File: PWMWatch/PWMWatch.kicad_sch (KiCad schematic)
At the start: 22 parts, among them J1 USB_C_Receptacle_USB2.0_14P, SW1 RST, SW2 BOOT, U1 STM32WB50CGUx, U2 NCP1117-3.3_SOT223, U3 TVS1400DRV

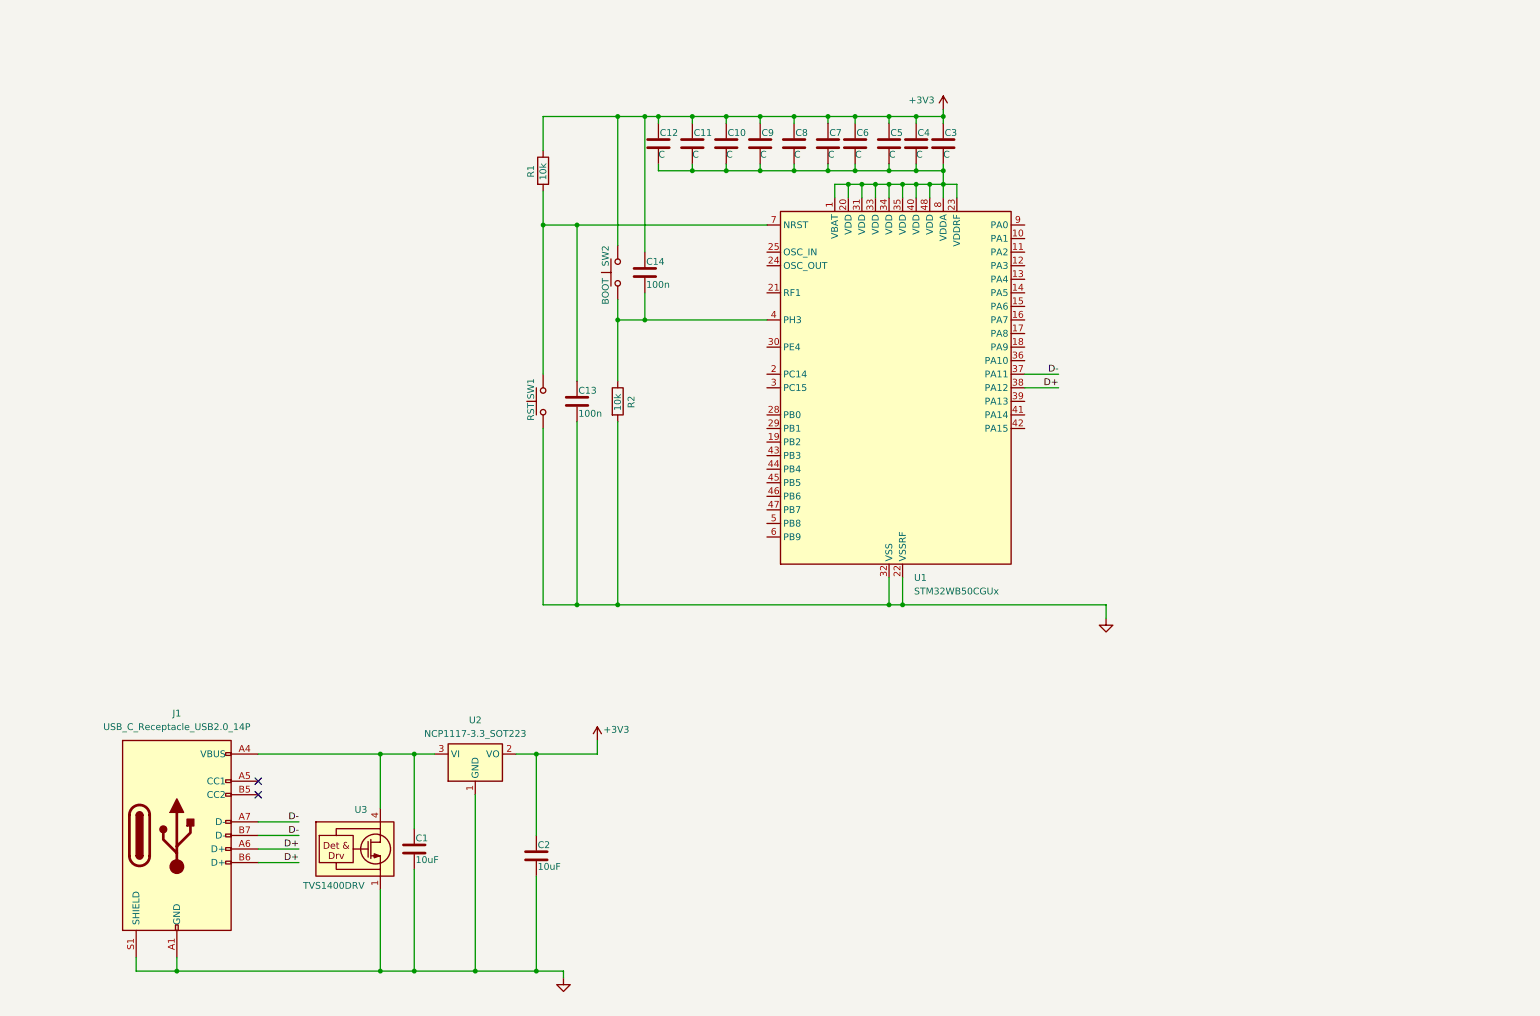
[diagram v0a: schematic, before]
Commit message: Added RTC
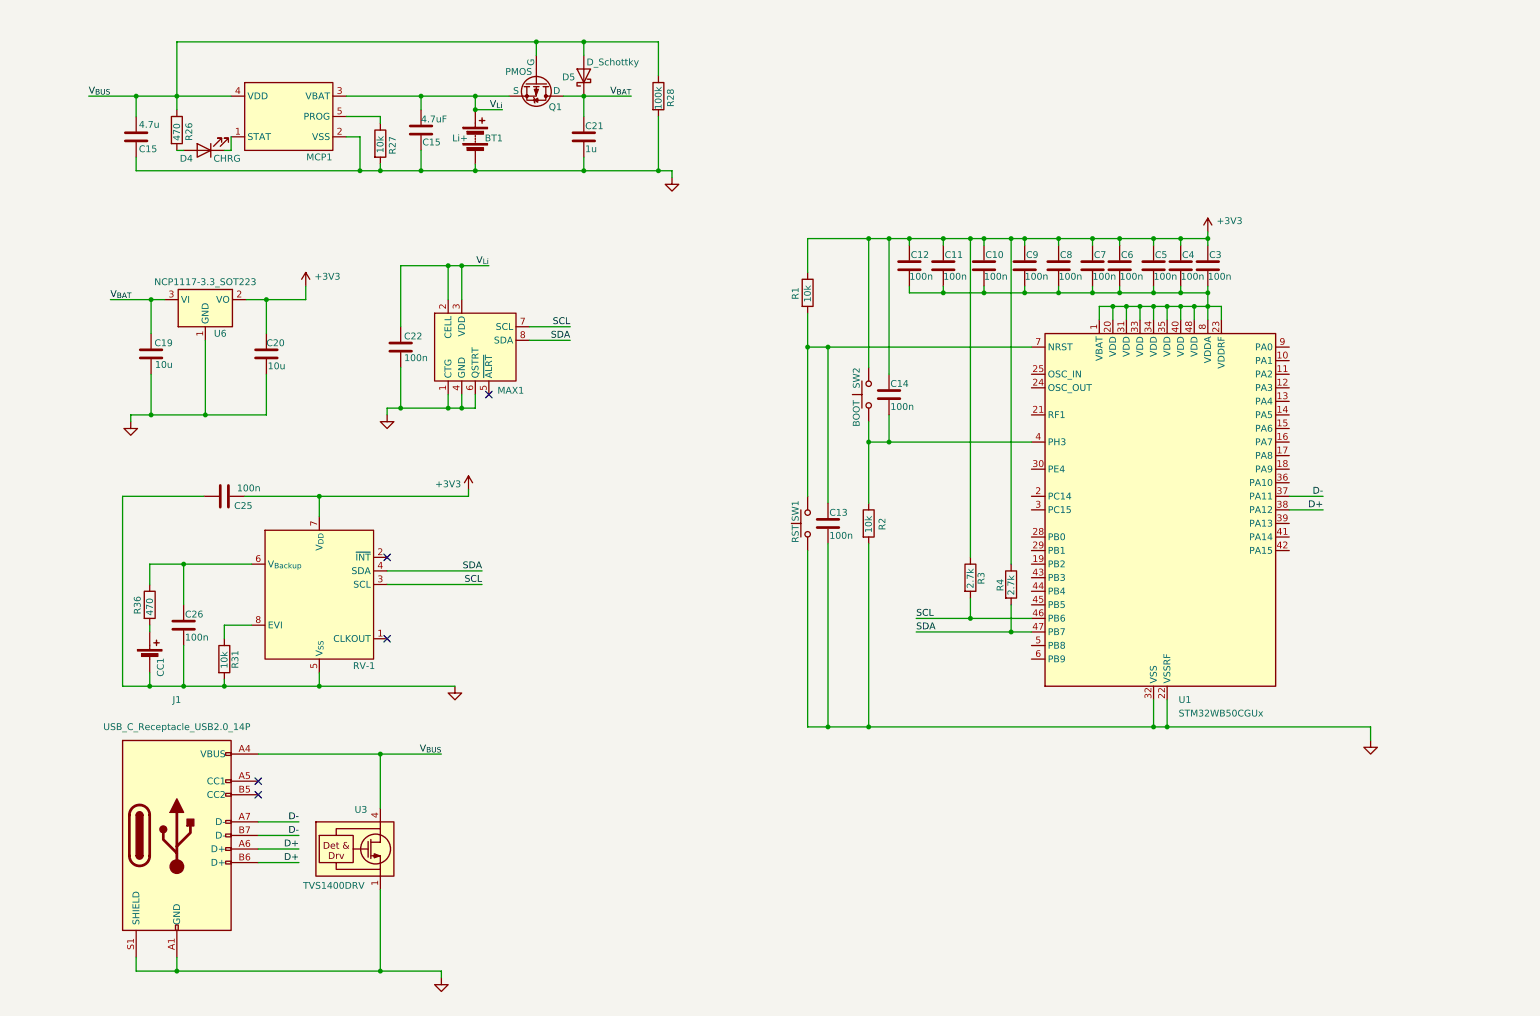
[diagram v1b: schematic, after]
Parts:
- removed C1, C2: 10uF, symbol Device:C
- removed U2: NCP1117-3.3_SOT223, Package_TO_SOT_SMD:SOT-223-3_TabPin2, symbol Regulator_Linear:NCP1117-3.3_SOT223
- added BT1: Li+, symbol Device:Battery
- added C15: 4.7u, Capacitor_SMD:C_0603_1608Metric, symbol Device:C
- added C15: 4.7uF, Capacitor_SMD:C_0603_1608Metric, symbol Device:C
- added C19, C20: 10u, Capacitor_SMD:C_0805_2012Metric, symbol Device:C
- added C21: 1u, Capacitor_SMD:C_0805_2012Metric, symbol Device:C
- added C22, C25, C26: 100n, Capacitor_SMD:C_0805_2012Metric, symbol Device:C
- added CC1: Battery_Cell, Uni:BAT_BK-414, symbol Device:Battery_Cell
- added D4: CHRG, LED_SMD:LED_0603_1608Metric, symbol Device:LED
- added D5: D_Schottky, Diode_SMD:D_SOD-123, symbol Device:D_Schottky
- added MAX1: ~, Package_DFN_QFN:TDFN-8-1EP_2x2mm_P0.5mm_EP0.8x1.2mm, symbol MAX17048:MAX17048
- added MCP1: ~, Package_TO_SOT_SMD:SOT-23-5, symbol MCP7383:MCP7383
- added Q1: PMOS, Package_TO_SOT_SMD:SOT-23-3, symbol Simulation_SPICE:PMOS
- added R26, R36: 470, Resistor_SMD:R_0603_1608Metric, symbol Device:R
- added R27, R31: 10k, Resistor_SMD:R_0603_1608Metric, symbol Device:R
- added R28: 100k, Resistor_SMD:R_0603_1608Metric, symbol Device:R
- added R3, R4: 2.7k, symbol Device:R
- added RV-1: ~, Uni:IC_RV-3028-C8-32.768KHZ-1PPM-TA-QC, symbol RV3028:RV-3028
- added U6: NCP1117-3.3_SOT223, Package_TO_SOT_SMD:SOT-223-3_TabPin2, symbol Regulator_Linear:NCP1117-3.3_SOT223
- C10, C11, C12, C3, C4, C5, C6, C7, C8, C9: value C -> 100n
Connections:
- net +3V3: now also C20.2, C25.2, R3.1, R4.1, RV-1.7 (V_{DD}), U6.2 (VO)
- net GND: now also BT1.2 (-), C15.2, C15.2, C19.1, C20.1, C21.2, C22.1, C25.1, C26.2, CC1.2 (-), MAX1.1 (CTG), MAX1.4 (GND), MAX1.6 (QSTRT), MCP1.2 (VSS), R27.2, R28.2, R31.2, RV-1.5 (V_{SS}), U6.1 (GND)
- net SCL: now reaches U1.46 (PB6)
- net SCL: now also MAX1.7 (SCL), R3.2, RV-1.3 (SCL)
- net SDA: now reaches U1.47 (PB7)
- net SDA: now also MAX1.8 (SDA), R4.2, RV-1.4 (SDA)
- net V_{BUS}: now reaches J1.A4 (VBUS), J1.A9 (VBUS), J1.B4 (VBUS), J1.B9 (VBUS), U3.4 (IN), U3.5 (IN), U3.6 (IN)
- net V_{BUS}: now also C15.1, D5.2 (A), MCP1.4 (VDD), Q1.2 (G), R26.1, R28.1
- new net: C26.1, R36.1, RV-1.6 (V_{Backup})
- new net: D4.1 (K), MCP1.1 (STAT)
- new net: D4.2 (A), R26.2
- new net: CC1.1 (+), R36.2
- new net: MCP1.5 (PROG), R27.1
- new net: R31.1, RV-1.8 (EVI)
- new net V_{BAT}: C19.2, C21.1, D5.1 (K), Q1.1 (D), U6.3 (VI)
- new net V_{Li}: BT1.1 (+), C15.1, C22.2, MAX1.2 (CELL), MAX1.3 (VDD), MCP1.3 (VBAT), Q1.3 (S)
- no-connect marks 2 -> 5
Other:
- moved on the sheet: C10, C11, C12, C13, C14, C3, C4, C5, C6, C7, C8, C9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

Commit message: magnetic encoder + buttons + organization of schematic
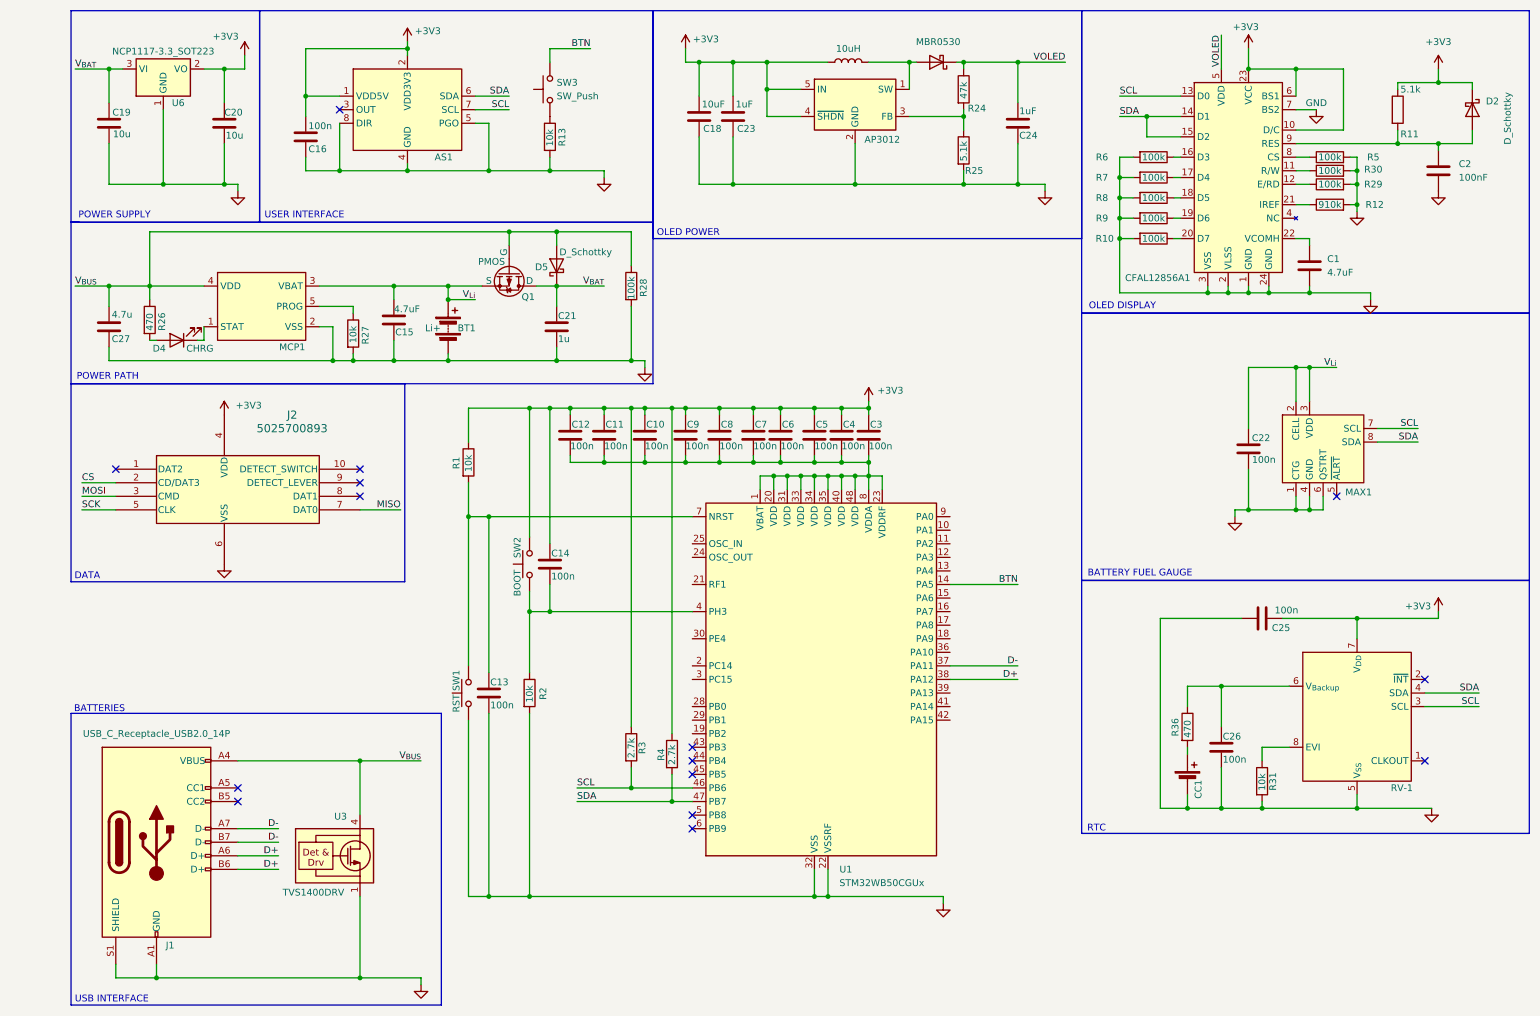
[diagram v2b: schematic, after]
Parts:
- added AS1: ~, Package_SO:SOIC-8_3.9x4.9mm_P1.27mm, symbol AS5600:AS5600
- added C1: 4.7uF, Capacitor_SMD:C_1206_3216Metric, symbol Device:C
- added C16: 100n, Capacitor_SMD:C_0805_2012Metric, symbol Device:C
- added C18: 10uF, Capacitor_SMD:C_0805_2012Metric, symbol Device:C
- added C2: 100nF, Capacitor_SMD:C_0805_2012Metric, symbol Device:C
- added C23, C24: 1uF, Capacitor_SMD:C_0805_2012Metric, symbol Device:C
- added CFAL12856A1: ~, Uni:GCT_FFC2A32-24-T, symbol CFAL128:CFAL128
- added D2: D_Schottky, Diode_SMD:D_SOD-523, symbol Device:D_Schottky
- added D6: MBR0530, Diode_SMD:D_SOD-123, symbol Diode:MBR0530
- added J2: 5025700893, Uni:GCT_MEM2061-01-188-00-A_REVA, symbol 2025-07-06_05-28-46:5025700893
- added L2: 10uH, Uni:IND_TAIYO_NRS4018_TAY, symbol Device:L
- added R10, R29, R30, R5, R6, R7, R8, R9: 100k, Resistor_SMD:R_0603_1608Metric, symbol Device:R
- added R11, R25: 5.1k, Resistor_SMD:R_0603_1608Metric, symbol Device:R
- added R12: 910k, Resistor_SMD:R_0603_1608Metric, symbol Device:R
- added R13: 10k, symbol Device:R
- added R24: 47k, Resistor_SMD:R_0603_1608Metric, symbol Device:R
- added SW3: SW_Push, symbol Switch:SW_Push
- added U2: AP3012, Package_TO_SOT_SMD:SC-74A-5_1.55x2.9mm_P0.95mm, symbol Regulator_Switching:AP3012
- C10, C11, C12, C13, C14, C3, C4, C5, C6, C7, C8, C9: footprint (none) -> Capacitor_SMD:C_0805_2012Metric
- R1, R2, R3, R4: footprint (none) -> Capacitor_SMD:C_0603_1608Metric
- renumbered C15 to C27
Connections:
- net +3V3: now also AS1.1 (VDD5V), AS1.2 (VDD3V3), C16.1, C18.1, C23.1, CFAL12856A1.10 (D/C), CFAL12856A1.23 (VCC), CFAL12856A1.6 (BS1), D2.1 (K), J2.4 (VDD), L2.1, R11.1, U2.4 (~{SHDN}), U2.5 (IN)
- net GND: now also AS1.4 (GND), AS1.5 (PGO), AS1.8 (DIR), C1.2, C16.2, C18.2, C2.2, C23.2, C24.2, CFAL12856A1.1 (GND), CFAL12856A1.2 (VLSS), CFAL12856A1.24 (GND), CFAL12856A1.3 (VSS), CFAL12856A1.7 (BS2), J2.6 (VSS), R10.2, R12.2, R13.2, R25.2, R29.2, R30.2, R5.2, R6.2, R7.2, R8.2, R9.2, U2.2 (GND)
- net SCL: now also AS1.7 (SCL), CFAL12856A1.13 (D0)
- net SDA: now also AS1.6 (SDA), CFAL12856A1.14 (D1), CFAL12856A1.15 (D2)
- net BTN: now reaches U1.14 (PA5)
- net BTN: now also SW3.2
- new net: C1.1, CFAL12856A1.22 (VCOMH)
- new net: D6.2 (A), L2.2, U2.1 (SW)
- new net: R24.2, R25.1, U2.3 (FB)
- new net: CFAL12856A1.17 (D4), R7.1
- new net: R13.1, SW3.1
- new net: CFAL12856A1.11 (R/W), R30.1
- new net: CFAL12856A1.12 (E/RD), R29.1
- new net: CFAL12856A1.19 (D6), R9.1
- new net: CFAL12856A1.8 (CS), R5.1
- new net: C2.1, CFAL12856A1.9 (RES), D2.2 (A), R11.2
- new net: CFAL12856A1.16 (D3), R6.1
- new net: CFAL12856A1.18 (D5), R8.1
- new net: CFAL12856A1.21 (IREF), R12.1
- new net: CFAL12856A1.20 (D7), R10.1
- new net CS: J2.2 (CD/DAT3)
- new net MISO: J2.7 (DAT0)
- new net MOSI: J2.3 (CMD)
- new net SCK: J2.5 (CLK)
- new net VOLED: C24.1, CFAL12856A1.5 (VDD), D6.1 (K), R24.1
- no-connect marks 5 -> 15
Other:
- note added: "BATTERIES"
- note added: "BATTERY FUEL GAUGE"
- note added: "DATA"
- note added: "OLED DISPLAY"
- note added: "OLED POWER"
- note added: "POWER PATH"
- note added: "POWER SUPPLY"
- note added: "RTC"
- note added: "USB INTERFACE"
- note added: "USER INTERFACE"
- moved on the sheet: BT1, C10, C11, C12, C13, C14, C15, C19, C20, C21, C22, C25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

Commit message: footprints
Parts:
- BT1: footprint (none) -> Connector_JST:JST_PH_B2B-PH-K_1x02_P2.00mm_Vertical
- CC1: footprint Uni:BAT_BK-414 -> Watch:BAT_BK-414
- CFAL12856A1: footprint Uni:GCT_FFC2A32-24-T -> Watch:GCT_FFC2A32-24-T
- J1, SW1, SW2: footprint (none) -> Button_Switch_SMD:SW_Push_1P1T_NO_CK_KMR2
- J2: footprint Uni:GCT_MEM2061-01-188-00-A_REVA -> Watch:MOLEX_5025700893
- L2: footprint Uni:IND_TAIYO_NRS4018_TAY -> Watch:CDRH3D14HPNP100NC
- R13: footprint (none) -> Resistor_SMD:R_0603_1608Metric
- RV-1: footprint Uni:IC_RV-3028-C8-32.768KHZ-1PPM-TA-QC -> Watch:IC_RV-3028-C8-32.768KHZ-1PPM-TA-QC
- SW3: footprint (none) -> Watch:SW_EVQ-P7A01P
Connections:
- no-connect marks 15 -> 37
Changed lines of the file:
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@@
 	)
 	(no_connect
+		(at 176.53 124.46)
+	)
+	(no_connect
+		(at 176.53 129.54)
+	)
+	(no_connect
+		(at 176.53 121.92)
+	)
+	(no_connect
 		(at 128.27 154.94)
 	)
@@
 	)
 	(no_connect
+		(at 176.53 106.68)
+	)
+	(no_connect
+		(at 128.27 114.3)
+	)
+	(no_connect
 		(at 66.04 102.87)
 	)
 	(no_connect
+		(at 176.53 132.08)
+	)
+	(no_connect
+		(at 128.27 111.76)
+	)
+	(no_connect
 		(at 43.18 160.02)
 	)
 	(no_connect
+		(at 176.53 116.84)
+	)
+	(no_connect
+		(at 128.27 147.32)
+	)
+	(no_connect
+		(at 128.27 144.78)
+	)
+	(no_connect
+		(at 176.53 139.7)
+	)
+	(no_connect
 		(at 128.27 165.1)
 	)
@@
 	)
 	(no_connect
+		(at 128.27 119.38)
+	)
+	(no_connect
+		(at 128.27 137.16)
+	)
+	(no_connect
 		(at 128.27 152.4)
 	)
 	(no_connect
+		(at 176.53 109.22)
+	)
+	(no_connect
 		(at 265.43 152.4)
 	)
 	(no_connect
+		(at 128.27 134.62)
+	)
+	(no_connect
 		(at 62.23 30.48)
 	)
@@
 		(at 128.27 149.86)
 	)
+	(no_connect
+		(at 176.53 144.78)
+	)
+	(no_connect
+		(at 128.27 129.54)
+	)
+	(no_connect
+		(at 128.27 142.24)
+	)
+	(no_connect
+		(at 176.53 114.3)
+	)
+	(no_connect
+		(at 176.53 127)
+	)
+	(no_connect
+		(at 176.53 111.76)
+	)
+	(no_connect
+		(at 176.53 142.24)
+	)
 	(wire
 		(pts
@@
 			)
 		)
-		(property "Footprint" ""
+		(property "Footprint" "Button_Switch_SMD:SW_Push_1P1T_NO_CK_KMR2"
 			(at 92.71 115.57 0)
 			(effects
@@
 			)
 		)
-		(property "Footprint" ""
+		(property "Footprint" "Resistor_SMD:R_0603_1608Metric"
 			(at 99.822 35.56 90)
 			(effects
@@
 			)
 		)
-		(property "Footprint" ""
+		(property "Footprint" "Button_Switch_SMD:SW_Push_1P1T_NO_CK_KMR2"
 			(at 81.28 139.7 0)
 			(effects
@@
 			)
 		)
-		(property "Footprint" "Uni:GCT_MEM2061-01-188-00-A_REVA"
+		(property "Footprint" "Watch:MOLEX_5025700893"
 			(at 20.32 97.79 0)
 			(effects
@@
 			)
 		)
-		(property "Footprint" "Uni:BAT_BK-414"
+		(property "Footprint" "Watch:BAT_BK-414"
 			(at 220.98 154.686 90)
 			(effects
@@
 			)
 		)
-		(property "Footprint" ""
+		(property "Footprint" "Button_Switch_SMD:SW_Push_1P1T_NO_CK_KMR2"
 			(at 31.75 167.64 0)
 			(effects
@@
 			)
 		)
-		(property "Footprint" ""
+		(property "Footprint" "Watch:SW_EVQ-P7A01P"
 			(at 96.52 26.67 0)
 			(effects
@@
 			)
 		)
-		(property "Footprint" "Uni:IND_TAIYO_NRS4018_TAY"
+		(property "Footprint" "Watch:CDRH3D14HPNP100NC"
 			(at 157.48 21.59 0)
 			(effects
@@
 			)
 		)
-		(property "Description" "Inductor"
+		(property "Description" "CDRH3D14"
 			(at 157.48 21.59 0)
 			(effects
@@
 			)
 		)
-		(property "Footprint" "Uni:GCT_FFC2A32-24-T"
+		(property "Footprint" "Watch:GCT_FFC2A32-24-T"
 			(at 229.87 49.53 0)
 			(effects
@@
 			)
 		)
-		(property "Footprint" "Uni:IC_RV-3028-C8-32.768KHZ-1PPM-TA-QC"
+		(property "Footprint" "Watch:IC_RV-3028-C8-32.768KHZ-1PPM-TA-QC"
 			(at 230.886 136.398 0)
 			(effects
@@
 			)
 		)
-		(property "Footprint" ""
+		(property "Footprint" "Connector_JST:JST_PH_B2B-PH-K_1x02_P2.00mm_Vertical"
 			(at 82.55 69.596 90)
 			(effects

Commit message: usb
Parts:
- J1: footprint Button_Switch_SMD:SW_Push_1P1T_NO_CK_KMR2 -> Connector_USB:USB_C_Receptacle_GCT_USB4105-xx-A_16P_TopMnt_Horizontal
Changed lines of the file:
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@@
 			)
 		)
-		(property "Footprint" "Button_Switch_SMD:SW_Push_1P1T_NO_CK_KMR2"
+		(property "Footprint" "Connector_USB:USB_C_Receptacle_GCT_USB4105-xx-A_16P_TopMnt_Horizontal"
 			(at 31.75 167.64 0)
 			(effects
@@
 					(size 1.27 1.27)
 				)
-				(hide yes)
 			)
 		)

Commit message: placements + fixed all the wrong footprints
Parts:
- added R14, R15: 5.1k, Resistor_SMD:R_0603_1608Metric, symbol Device:R_Small
- AS1, CFAL12856A1, MAX1, MCP1, RV-1: value ~ -> (none)
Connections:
- net GND: now also R14.2, R15.2
- net at J1.A5 (CC1): now also R14.1
- net at J1.B5 (CC2): now also R15.1
- no-connect marks 37 -> 35
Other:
- moved on the sheet: SW3

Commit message: pcb done 4th time
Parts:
- added R16, R17, R18: 10k, Resistor_SMD:R_0603_1608Metric, symbol Device:R
- BT1: footprint Connector_JST:JST_PH_B2B-PH-K_1x02_P2.00mm_Vertical -> Watch:CONN_BM02B-SRSS-TB_JST
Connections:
- net +3V3: now also R16.1, R17.1, R18.1
- net BTN: now also U1.13 (PA4); no longer U1.14 (PA5)
- net MISO: now also U1.15 (PA6), R17.2
- net MOSI: now also U1.16 (PA7), R18.2
- net SCK: now also U1.14 (PA5), R16.2
- no-connect marks 35 -> 32

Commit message: all the stuff done
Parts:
- CC1: footprint Watch:BAT_BK-414 -> Watch:BAT_2994
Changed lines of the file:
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@@
 			)
 		)
-		(property "Footprint" "Watch:BAT_BK-414"
+		(property "Footprint" "Watch:BAT_2994"
 			(at 220.98 154.686 90)
 			(hide yes)
